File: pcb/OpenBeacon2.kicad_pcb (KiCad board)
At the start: 4 copper layers, 120 x 100 mm, 265 parts, among them J1 Bias V, J10 UART, J11 BNC, J12 USB_C_Receptacle, J13 UPDI, J14 PPS, J15 U.FL, J16 SMA CLKIN, J2 PAI+, J3 PAI-, J4 Digital IO, J5 ADC Inputs, J6 SMA, J8 I2C Bus, J9 GND, K1 G6K-2F-Y-DC5, K2 G6K-2F-Y-DC5, K3 G6K-2F-Y-DC5, K4 G6K-2F-Y-DC5, K5 G6K-2F-Y-DC5, K6 G6K-2F-Y-DC5, Q1 2N7002, Q2 MMBT4403, Q3 BS170, Q4 2N7002, Q5 2N7002, Q6 AO3400A, Q7 AO3400A, Q8 BS170, U1 TLV61046A, U10 CP2102N-A02-GQFN24, U11 TLV75533PDBV, U12 MAX-M10S-00B, U13 TPS22941, U2 25.000 MHz TCXO, U3 SN74LVC1G17, U4 SI5351C-B-GMR, U5 MCP4725A1T-E/CH, U8 24AA64T, U9 AVR128DA48-E/PT, Y1 32.768kHz

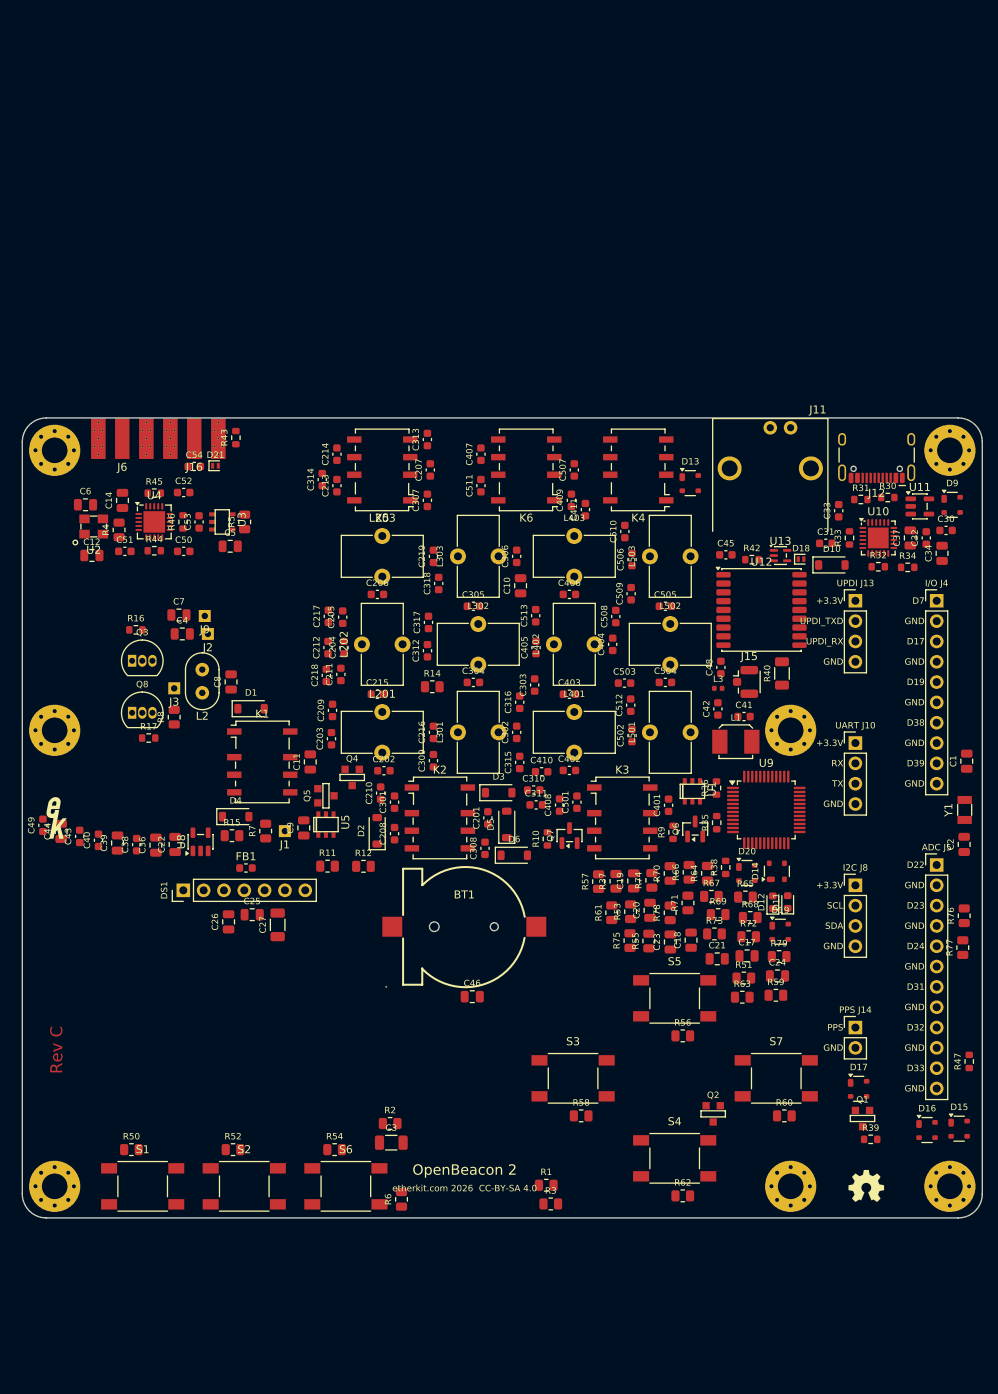
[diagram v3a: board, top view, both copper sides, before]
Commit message: PCB Rev C: tighter filter bank, USB-C J12 to back-left by SMAs, GPS moved away from RF chain, drop VFO holes H1/H2/H4, reference silk moved outside bodies
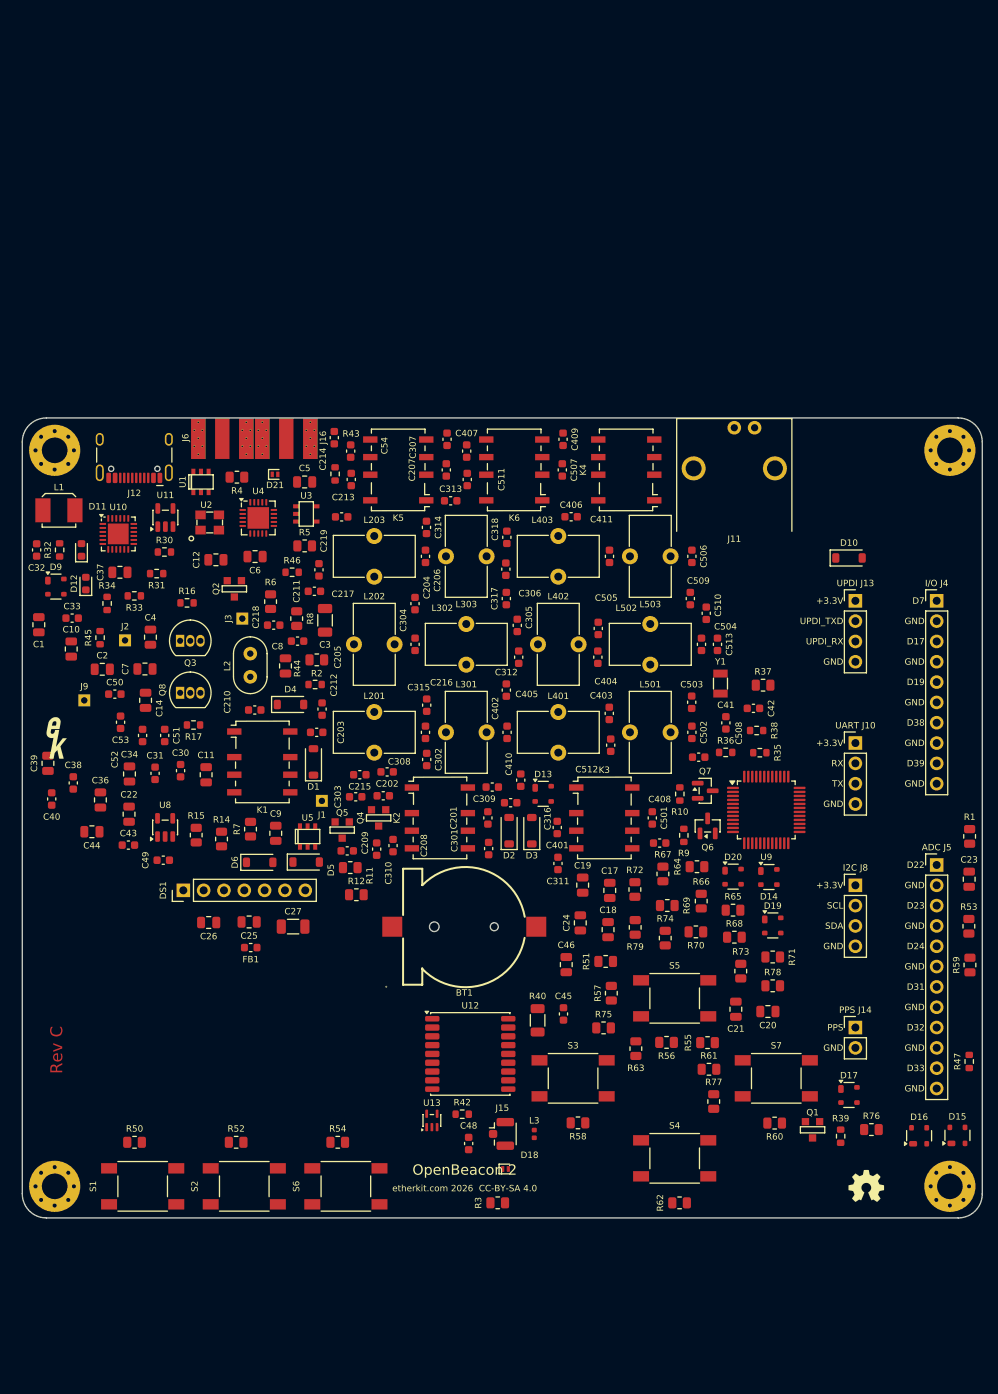
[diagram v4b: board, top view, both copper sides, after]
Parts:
- removed H1, H2, H4: MountingHole_M3, MountingHole:MountingHole_3.2mm_M3_Pad_Via
- moved C1 117.2 mm to (102.1, 125.9)
- moved D9 112.5 mm to (104.2, 121.1)
- moved C32 111.2 mm to (101.8, 116.5)
- moved C2 109.9 mm to (110.0, 131.4), turned to 0 degrees
- moved C34 105.2 mm to (113.4, 144.5)
- moved R32 102.4 mm to (104.7, 116.5), turned to 90 degrees
- moved C30 100.3 mm to (119.8, 144.1), turned to 90 degrees
- moved R34 100.2 mm to (110.6, 123.2), turned to 90 degrees
- moved C37 98.9 mm to (112.2, 119.3), turned to 0 degrees
- moved D11 98.6 mm to (107.4, 116.5)
- moved C33 96.8 mm to (106.2, 125.0), turned to 0 degrees
- moved U10 95.0 mm to (112.0, 114.5)
- moved D12 94.7 mm to (107.9, 120.7)
- moved U11 94.3 mm to (117.9, 112.4), turned to 90 degrees
- moved J12 92.8 mm to (114.0, 103.8)
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
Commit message: PCB Rev C: nudge L503 clear of J11, VFO-style branding block with Etherkit+OSHW logos at front-right, Rev C on F.Cu at 0 deg
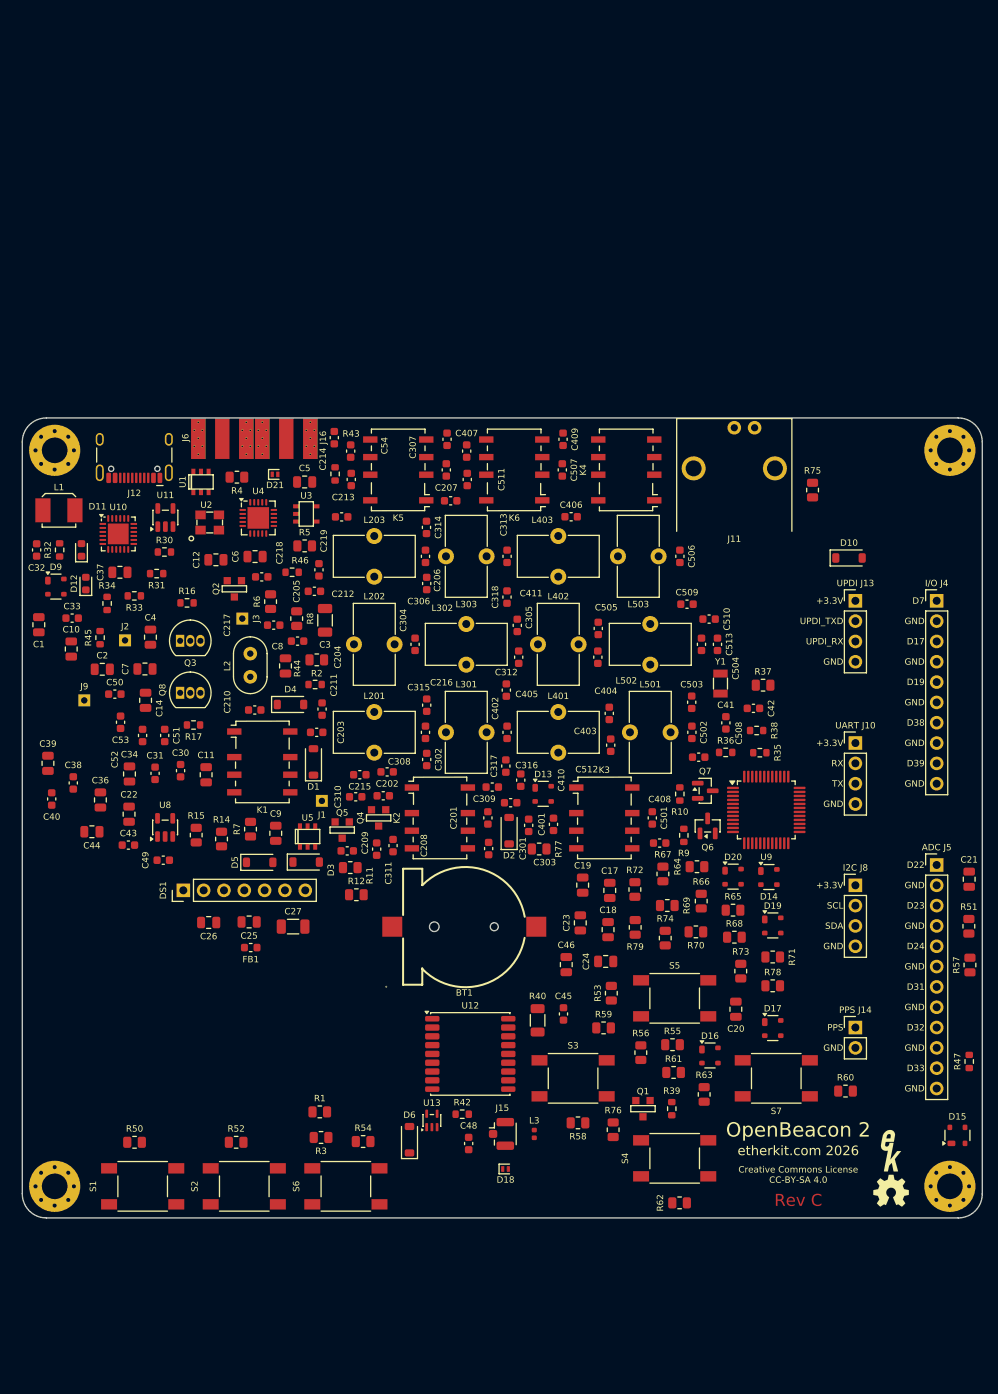
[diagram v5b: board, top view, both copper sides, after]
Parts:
- moved LOGO1 116.4 mm to (208.6, 191.6)
- moved R1 88.2 mm to (137.2, 186.7), turned to 0 degrees
- moved R75 72.1 mm to (198.8, 109.0), turned to 90 degrees
- moved C23 48.9 mm to (169.8, 163.1)
- moved R59 46.5 mm to (172.7, 176.2), turned to 0 degrees
- moved R51 45.6 mm to (218.3, 163.5), turned to 90 degrees
- moved R53 45.5 mm to (173.6, 171.9)
- moved R57 45.0 mm to (218.5, 168.4)
- moved D6 39.4 mm to (148.4, 190.2), turned to 90 degrees
- moved R77 38.4 mm to (164.6, 153.9), turned to 0 degrees
- moved C21 33.4 mm to (218.4, 157.7)
- moved R76 32.3 mm to (173.9, 189.0), turned to 90 degrees
- moved D3 28.5 mm to (135.5, 155.5), turned to 0 degrees
- moved D16 28.0 mm to (186.0, 179.7), turned to 0 degrees
- moved R3 23.5 mm to (137.3, 189.9)
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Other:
- board text added: "Creative Commons License CC-BY-SA 4.0"
- board text added: "etherkit.com 2026"
- board text removed: "etherkit.com 2026 CC-BY-SA 4.0"

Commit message: PCB Rev C: GPS U.FL J15 + U12 to back-left edge beside USB-C, away from PA/filters/J11
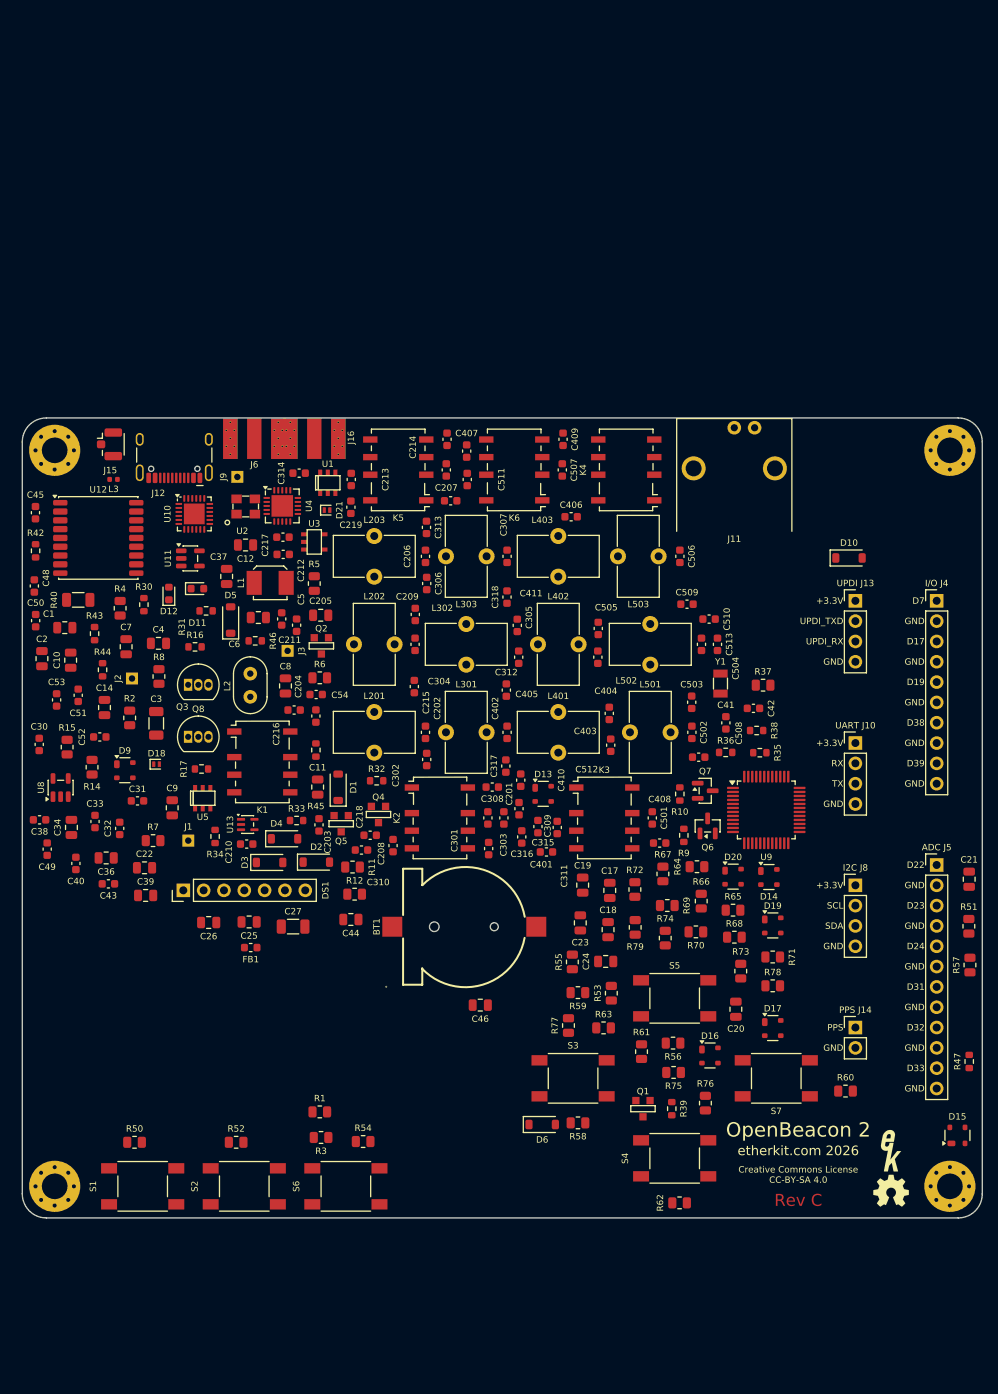
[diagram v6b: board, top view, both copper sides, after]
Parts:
- moved J15 99.2 mm to (111.4, 103.3)
- moved L3 97.3 mm to (111.4, 107.7), turned to 0 degrees
- moved C45 91.0 mm to (101.6, 111.8)
- moved C48 88.3 mm to (101.5, 121.0)
- moved R42 88.3 mm to (101.7, 116.6), turned to 90 degrees
- moved U12 79.5 mm to (109.5, 115.0)
- moved R40 77.8 mm to (107.0, 122.7), turned to 0 degrees
- moved R75 74.8 mm to (181.4, 181.8), turned to 0 degrees
- moved D18 66.8 mm to (116.8, 143.3)
- moved R32 49.0 mm to (144.3, 145.4), turned to 0 degrees
- moved U13 43.6 mm to (128.2, 150.8), turned to 0 degrees
- moved C32 36.3 mm to (112.2, 151.3)
- moved R43 36.1 mm to (109.0, 127.0)
- moved C54 34.9 mm to (136.7, 137.3)
- moved R33 34.6 mm to (134.3, 150.3)
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
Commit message: PCB Rev C: toroid column pitch 11.5->15 mm, PA beside K1, BT1 down, strict silk (no refs on courtyards), test-point function labels
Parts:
- moved C34 81.7 mm to (174.5, 106.5)
- moved R15 77.6 mm to (172.8, 102.3), turned to 0 degrees
- moved R63 72.6 mm to (213.1, 115.9), turned to 90 degrees
- moved R61 72.6 mm to (209.5, 114.1)
- moved R75 72.4 mm to (218.4, 119.6), turned to 90 degrees
- moved D5 49.5 mm to (164.7, 156.1), turned to 0 degrees
- moved R57 49.2 mm to (170.0, 176.6), turned to 0 degrees
- moved C19 48.9 mm to (218.4, 166.3)
- moved C21 47.8 mm to (173.8, 175.1)
- moved R53 44.8 mm to (218.4, 171.1)
- moved R51 43.7 mm to (177.5, 179.0)
- moved R74 38.7 mm to (218.4, 158.1)
- moved D6 38.4 mm to (166.8, 150.0), turned to 90 degrees
- moved U8 37.8 mm to (140.3, 159.2)
- moved R55 37.7 mm to (202.9, 184.0), turned to 0 degrees
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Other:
- board text added: "BIAS"
- board text added: "PAI+"
- board text added: "PAI-"
